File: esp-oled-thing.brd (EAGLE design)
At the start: 34.3 x 27 mm, 19 parts, among them IC1 REG1117

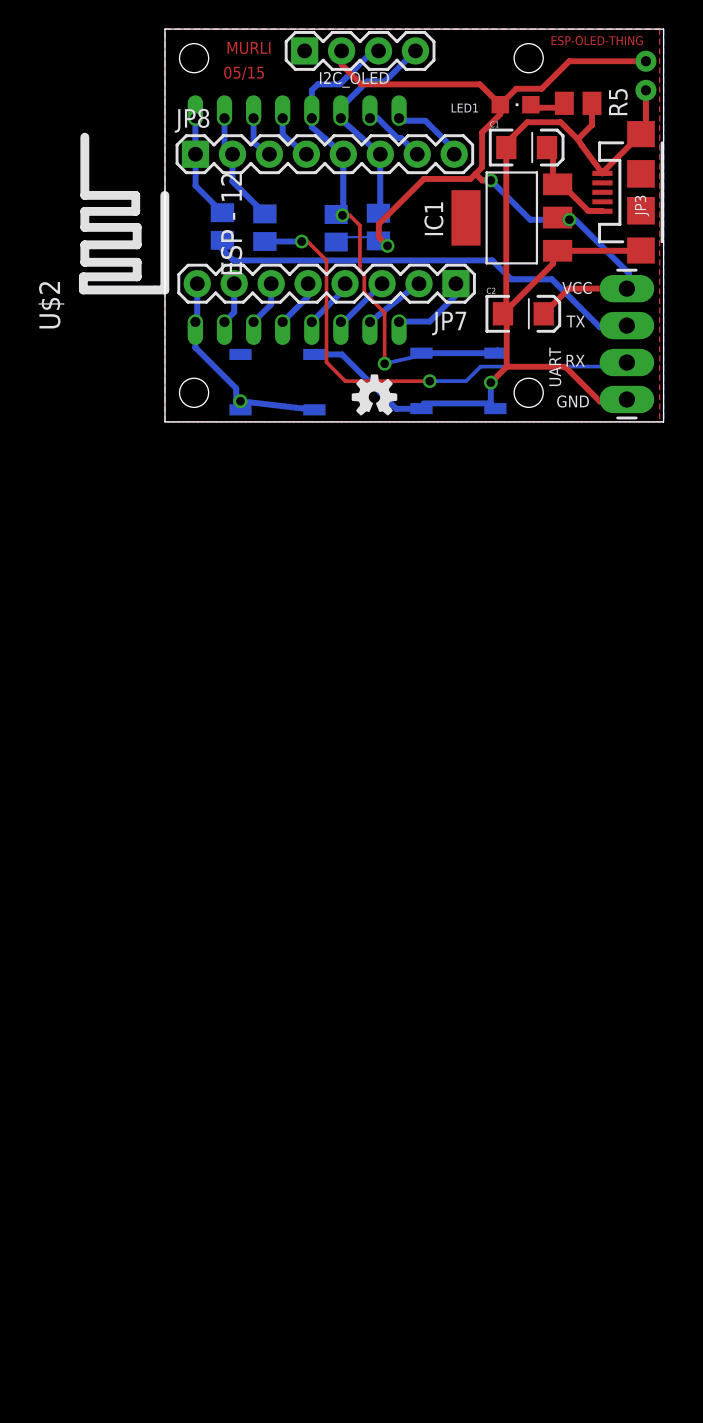
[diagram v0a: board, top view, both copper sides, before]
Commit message: tps61200 and mcp73831 for better lipo battery support added, usb connector changed to a more sturdier form factor
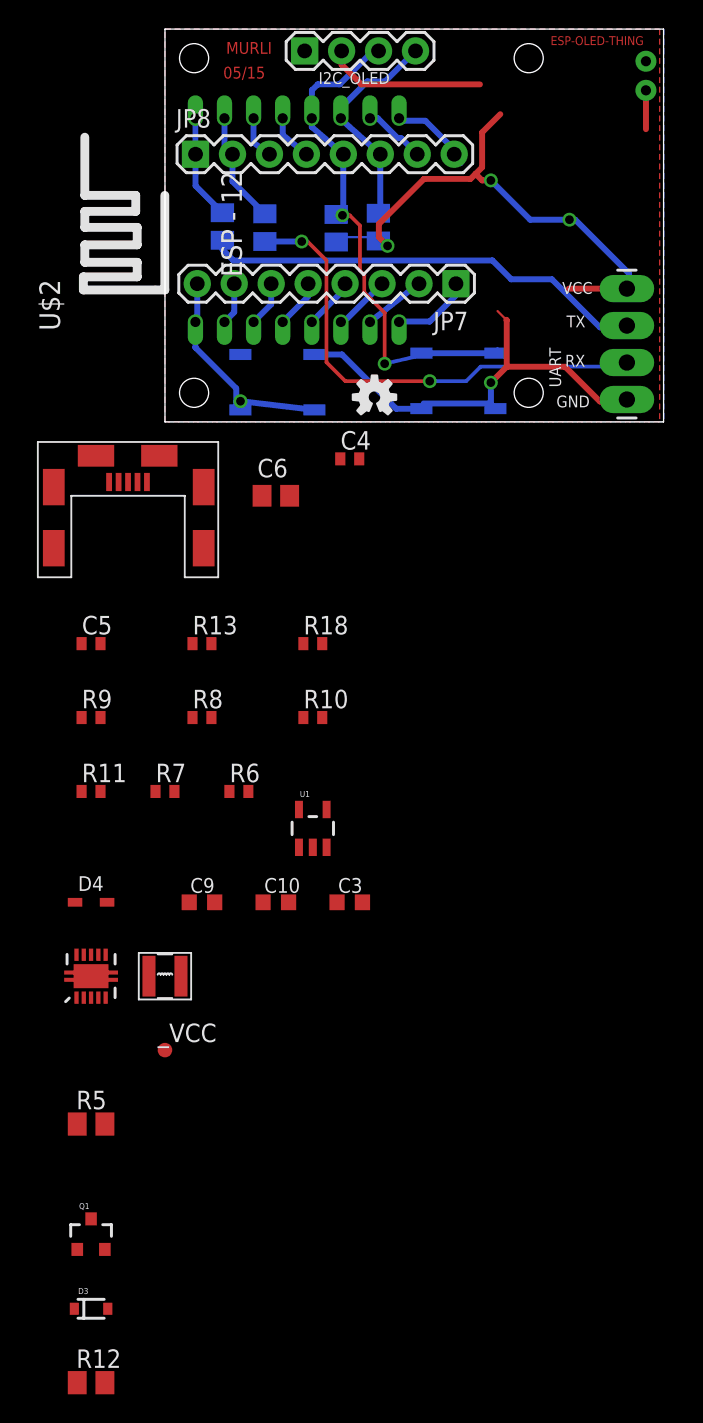
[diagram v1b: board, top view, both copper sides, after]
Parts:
- removed C1, C2: 10uF, SparkFun-Capacitors:EIA3216
- removed IC1: REG1117, burr-brown:SOT223
- removed JP3: USB-MICROB, SparkFun-Connectors:USB-MICROB
- removed LED1: POWER, adafruit:CHIPLED_0805
- added C10, C9: 4.7uF, rcl:C0603K
- added C3: 22uF, rcl:C0603K
- added C4, C5: 0.1uF, rcl:C0402
- added C6: 10uF, rcl:C0805
- added D3: BAT20J, SparkFun-DiscreteSemi:SOD-323
- added D4: 1n4148, zetex:SOD323
- added Q1: 2.5A/30V, SparkFun-DiscreteSemi:SOT23-3
- added R10, R8: 220k, rcl:R0402
- added R11: 10k, rcl:R0402
- added R12: 10K, adafruit:M0805
- added R13: 100E, rcl:R0402
- added R18: 470E, rcl:R0402
- added R6: 2k, rcl:R0402
- added R7: 2M, rcl:R0402
- added R9: 1.2M, rcl:R0402
- added U$3: INDUCTOR-NR3015, farasbee:INDUCTOR-NR3015
- added U$4: MICROUSB-MIDMOUNT, farasbee:MICROUSB-MIDMOUNT-MOLEX
- added U1: MCP73831, SparkFun:SOT23-5
- added U2: TPS61200, SparkFun:QFN-10_PAD
- added _VCC: TPTP10R, testpad:TP10R
- R5: value 1.2K -> 0Ohm
- moved R5 77.7 mm to (-5.08, -48.3), turned to 0 degrees
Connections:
- removed net N$1: C1.A, IC1.3, JP3.VBUS
- removed net N$10: LED1.C, R5.2
- removed net N$3: JP7.7, U$2.ADC
- new net 5VIN: C9.1, U$4.+5VDC, U1.4
- new net CHARGER_STATUS: U1.1
- new net FB: R10.2, R9.1, U2.10
- new net GND1: R10.1, R8.1, U2.8, U2.9
- new net N$13: R6.1, U1.5
- new net N$14: U$3.P$2, U2.3
- new net N$18: C5.1, U2.1
- new net N$21: D4.2, R18.2
- new net TPS_EN: R11.1, U2.6
- new net UVLO: C4.2, R7.1, R8.2, U2.7
- new net VBAT: JP6.2, Q1.3, R12.2
- new net VBATT: C10.1, C4.1, C6.1, R13.2, R7.2, U$3.P$1, U1.3
- new net VIN: R13.1, U2.5
- new net VIN1: D3.C, Q1.2
- new net VUSB: D3.A, Q1.1
- net GND: now also C10.2, C3.2, C5.2, C6.2, C9.2, R11.2, R12.1, R18.1, R6.2, U$4.GND, U1.2, U2.11, U2.12, U2.13, U2.14, U2.15, U2.4; no longer C1.C, C2.C, IC1.1, JP3.GND, JP3.MT1, JP3.MT2
- net N$15: now also R5.2
- net VCC: now also C3.1, D4.1, JP7.7, R9.2, U$2.ADC, U2.2, _VCC.TP; no longer C2.A, IC1.2, JP6.2, LED1.A
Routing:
- net GND: track 75.1 -> 34.2 mm
- net VCC: track 66.4 -> 51.7 mm
- net N$1: track 7.52 -> 0.00 mm
- net N$3: track 2.91 -> 0.00 mm
- net N$10: track 2.50 -> 0.00 mm
